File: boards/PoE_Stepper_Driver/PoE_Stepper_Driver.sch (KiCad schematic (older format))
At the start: 37 parts, among them J4 Programming, J5 48V In, J6 12V, 3V3 Out, J7 PHY Data, J8 SPI Data, SW3 SW_Push, U3 STM32F407VETx, U4 NCP1117, U5 E48SC12010, Y1 8MHz

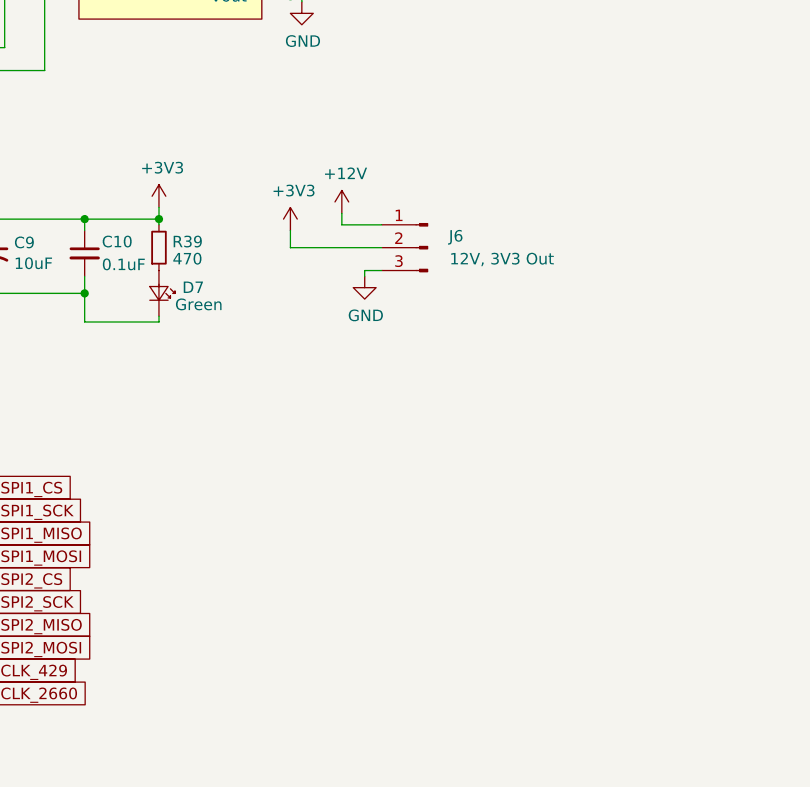
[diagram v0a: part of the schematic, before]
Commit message: finished 2660 planes
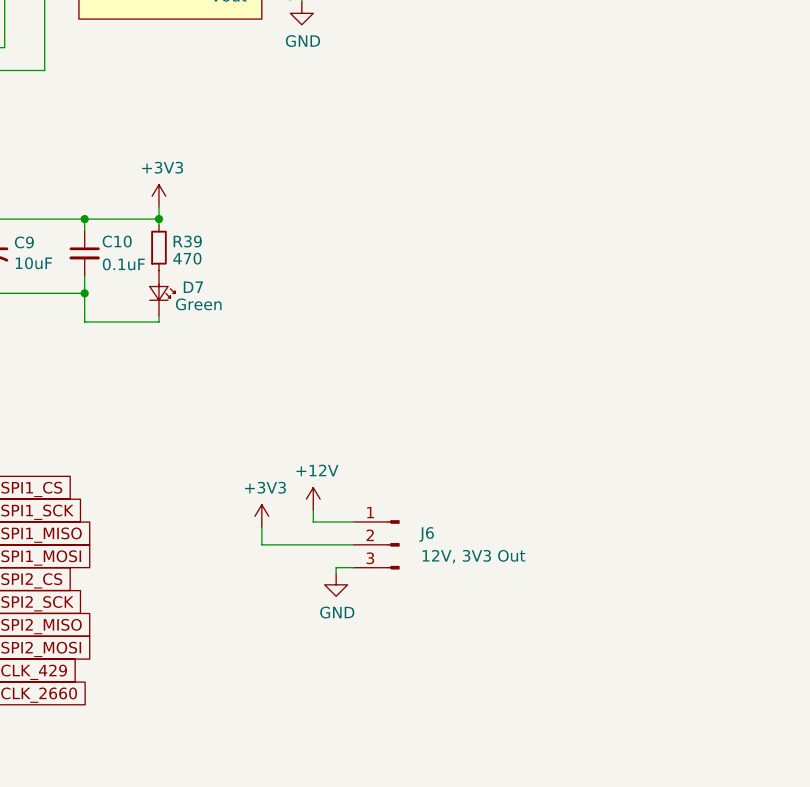
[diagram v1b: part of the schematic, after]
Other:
- moved on the sheet: J6
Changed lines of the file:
@@
 L Connector:Conn_01x03_Male J6
 U 1 1 6262632C
-P 10325 3475
+P 10200 4775
 AR Path="/6262632C" Ref="J6"  Part="1"
 AR Path="/620ECB3C/6262632C" Ref="J?"  Part="1"
-F 0 "J6" H 10200 3525 50  0000 C CNN
-F 1 "12V, 3V3 Out" H 10000 3425 50  0000 C CNN
-F 2 "Connector_PinHeader_2.54mm:PinHeader_1x03_P2.54mm_Vertical" H 10325 3475 50  0001 C CNN
-F 3 "~" H 10325 3475 50  0001 C CNN
-	1    10325 3475
+F 0 "J6" H 10075 4825 50  0000 C CNN
+F 1 "12V, 3V3 Out" H 9875 4725 50  0000 C CNN
+F 2 "Connector_PinHeader_2.54mm:PinHeader_1x03_P2.54mm_Vertical" H 10200 4775 50  0001 C CNN
+F 3 "~" H 10200 4775 50  0001 C CNN
+	1    10200 4775
 	-1   0    0    -1
 $EndComp
@@
 L power:GND #PWR058
 U 1 1 626508B2
-P 10050 3600
-F 0 "#PWR058" H 10050 3350 50  0001 C CNN
-F 1 "GND" H 10055 3427 50  0000 C CNN
-F 2 "" H 10050 3600 50  0001 C CNN
-F 3 "" H 10050 3600 50  0001 C CNN
-	1    10050 3600
+P 9925 4900
+F 0 "#PWR058" H 9925 4650 50  0001 C CNN
+F 1 "GND" H 9930 4727 50  0000 C CNN
+F 2 "" H 9925 4900 50  0001 C CNN
+F 3 "" H 9925 4900 50  0001 C CNN
+	1    9925 4900
 	1    0    0    -1
 $EndComp
 Wire Wire Line
-	10125 3575 10050 3575
+	10000 4875 9925 4875
 Wire Wire Line
-	10050 3575 10050 3600
+	9925 4875 9925 4900
 $Comp
 L power:+3V3 #PWR06
 U 1 1 6265E3AE
-P 9725 3400
-F 0 "#PWR06" H 9725 3250 50  0001 C CNN
-F 1 "+3V3" H 9740 3573 50  0000 C CNN
-F 2 "" H 9725 3400 50  0001 C CNN
-F 3 "" H 9725 3400 50  0001 C CNN
-	1    9725 3400
+P 9600 4700
+F 0 "#PWR06" H 9600 4550 50  0001 C CNN
+F 1 "+3V3" H 9615 4873 50  0000 C CNN
+F 2 "" H 9600 4700 50  0001 C CNN
+F 3 "" H 9600 4700 50  0001 C CNN
+	1    9600 4700
 	1    0    0    -1
 $EndComp
@@
 L power:+12V #PWR057
 U 1 1 626737A3
-P 9950 3325
-F 0 "#PWR057" H 9950 3175 50  0001 C CNN
-F 1 "+12V" H 9965 3498 50  0000 C CNN
-F 2 "" H 9950 3325 50  0001 C CNN
-F 3 "" H 9950 3325 50  0001 C CNN
-	1    9950 3325
+P 9825 4625
+F 0 "#PWR057" H 9825 4475 50  0001 C CNN
+F 1 "+12V" H 9840 4798 50  0000 C CNN
+F 2 "" H 9825 4625 50  0001 C CNN
+F 3 "" H 9825 4625 50  0001 C CNN
+	1    9825 4625
 	1    0    0    -1
 $EndComp
 Wire Wire Line
-	9950 3325 9950 3375
+	9825 4625 9825 4675
 Wire Wire Line
-	9950 3375 10125 3375
+	9825 4675 10000 4675
 Wire Wire Line
-	9725 3400 9725 3475
+	9600 4700 9600 4775
 Wire Wire Line
-	9725 3475 10125 3475
+	9600 4775 10000 4775
 Text GLabel 7450 5375 2    50   Input ~ 0
 CRS_DV
@@
 NoConn ~ 3225 6300
 $Comp
-L power:GND #PWR?
+L power:GND #PWR059
 U 1 1 628E2CDE
 P 2125 4050
-F 0 "#PWR?" H 2125 3800 50  0001 C CNN
+F 0 "#PWR059" H 2125 3800 50  0001 C CNN
 F 1 "GND" H 2130 3877 50  0000 C CNN
 F 2 "" H 2125 4050 50  0001 C CNN

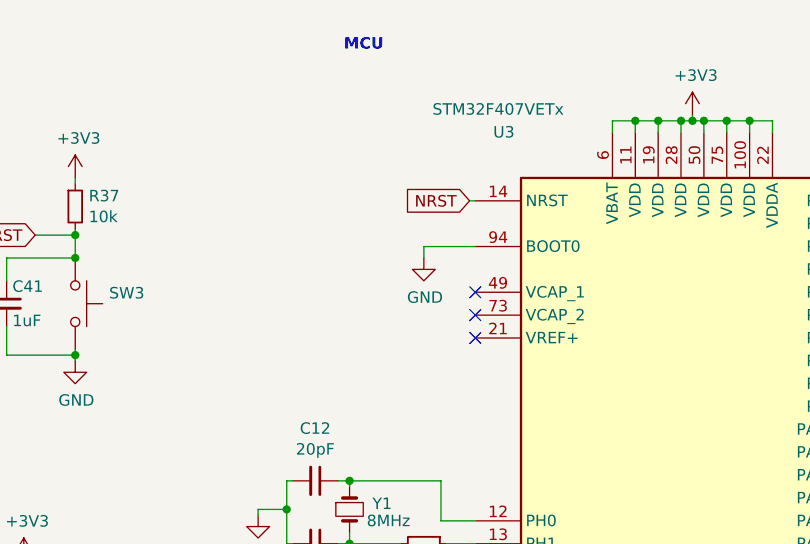
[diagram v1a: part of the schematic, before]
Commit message: added silkscreen info
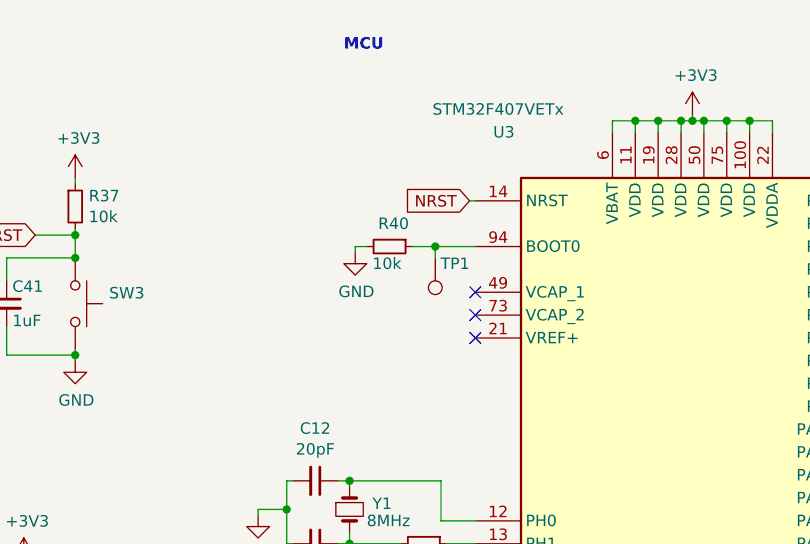
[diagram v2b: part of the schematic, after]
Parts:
- added R40: 10k, Resistor_SMD:R_0805_2012Metric_Pad1.15x1.40mm_HandSolder, symbol device:R_Small
- added TP1: BOOT0, TestPoint:TestPoint_Pad_1.0x1.0mm, symbol Connector:TestPoint
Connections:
- net GND: now also R40.2; no longer U3.94 (BOOT0)
- new net: R40.1, TP1.1, U3.94 (BOOT0)
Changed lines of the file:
@@
 L power:GND #PWR056
 U 1 1 625BB5F0
-P 3000 1750
-F 0 "#PWR056" H 3000 1500 50  0001 C CNN
-F 1 "GND" H 3005 1577 50  0000 C CNN
-F 2 "" H 3000 1750 50  0001 C CNN
-F 3 "" H 3000 1750 50  0001 C CNN
-	1    3000 1750
-	1    0    0    -1
-$EndComp
-Wire Wire Line
-	3225 1700 3000 1700
-Wire Wire Line
-	3000 1700 3000 1750
+P 2700 1725
+F 0 "#PWR056" H 2700 1475 50  0001 C CNN
+F 1 "GND" H 2705 1552 50  0000 C CNN
+F 2 "" H 2700 1725 50  0001 C CNN
+F 3 "" H 2700 1725 50  0001 C CNN
+	1    2700 1725
+	1    0    0    -1
+$EndComp
 $Comp
 L Connector:Conn_01x04_Male J4
@@
 	2125 3950 2125 4050
 Connection ~ 2125 3950
+$Comp
+L device:R_Small R40
+U 1 1 62AB9418
+P 2850 1700
+F 0 "R40" V 2750 1650 50  0000 L CNN
+F 1 "10k" V 2925 1625 50  0000 L CNN
+F 2 "Resistor_SMD:R_0805_2012Metric_Pad1.15x1.40mm_HandSolder" H 2850 1700 50  0001 C CNN
+F 3 "~" H 2850 1700 50  0001 C CNN
+	1    2850 1700
+	0    1    1    0
+$EndComp
+Wire Wire Line
+	2750 1700 2700 1700
+Wire Wire Line
+	2700 1700 2700 1725
+$Comp
+L Connector:TestPoint TP1
+U 1 1 62AE2994
+P 3050 1750
+F 0 "TP1" H 2900 1775 50  0000 L CNN
+F 1 "BOOT0" H 2775 1750 50  0001 L CNN
+F 2 "TestPoint:TestPoint_Pad_1.0x1.0mm" H 3250 1750 50  0001 C CNN
+F 3 "~" H 3250 1750 50  0001 C CNN
+	1    3050 1750
+	-1   0    0    1
+$EndComp
+Wire Wire Line
+	2950 1700 3050 1700
+Wire Wire Line
+	3050 1750 3050 1700
+Connection ~ 3050 1700
+Wire Wire Line
+	3050 1700 3225 1700
 $EndSCHEMATC

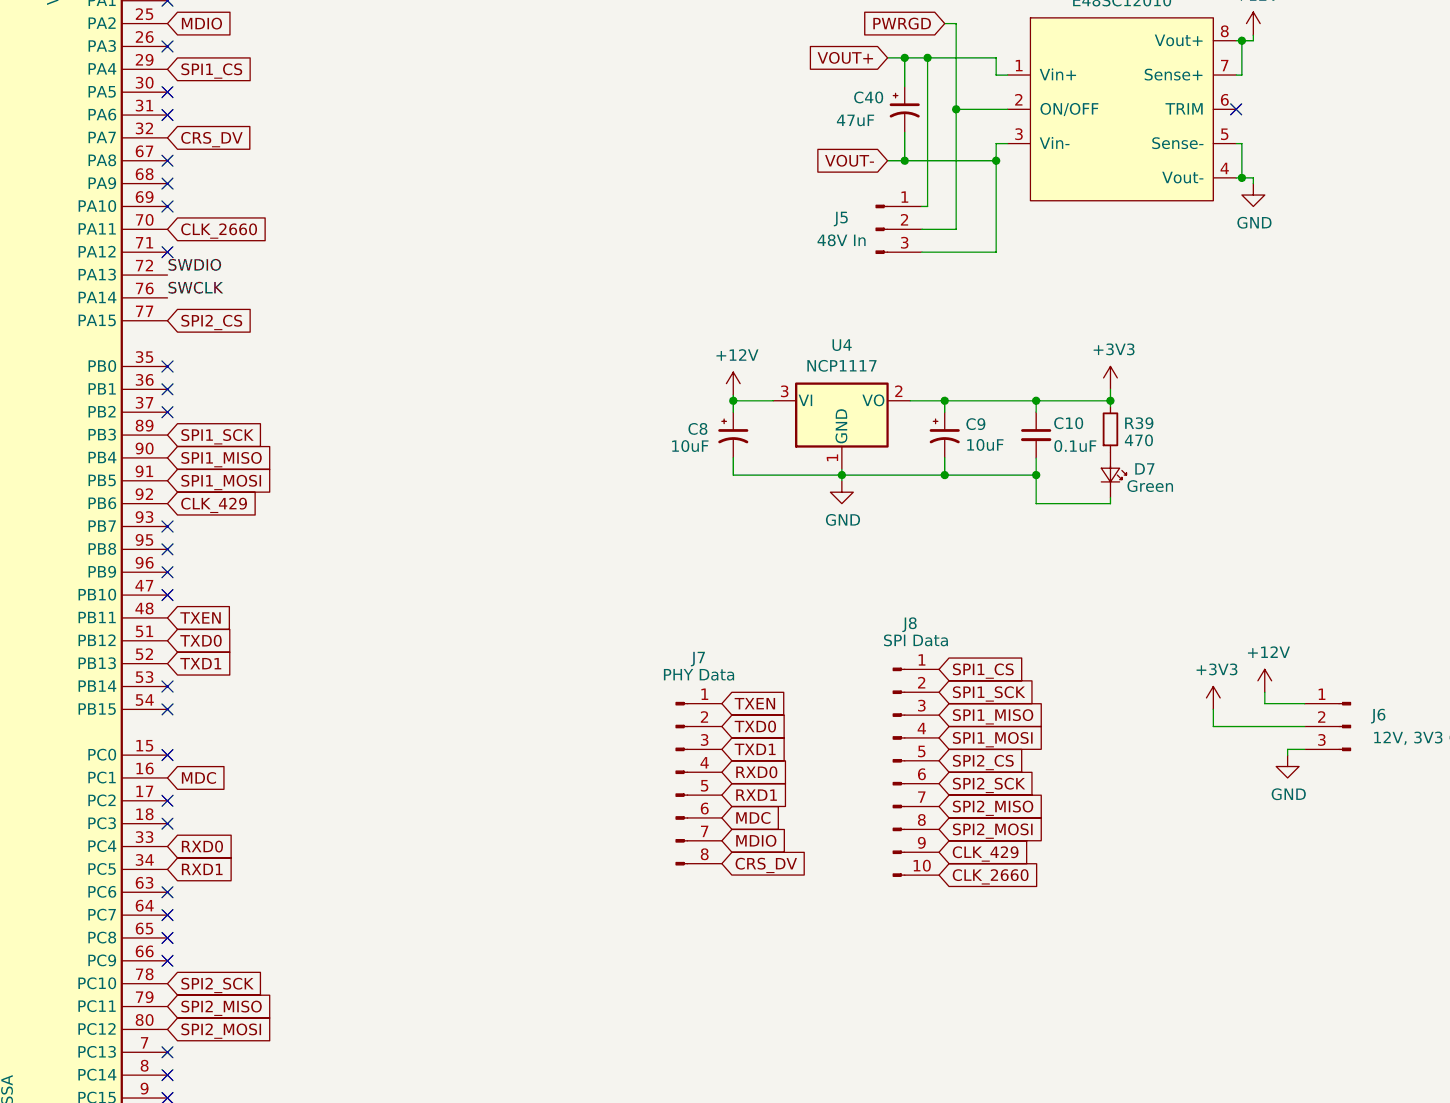
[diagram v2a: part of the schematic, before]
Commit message: added UART
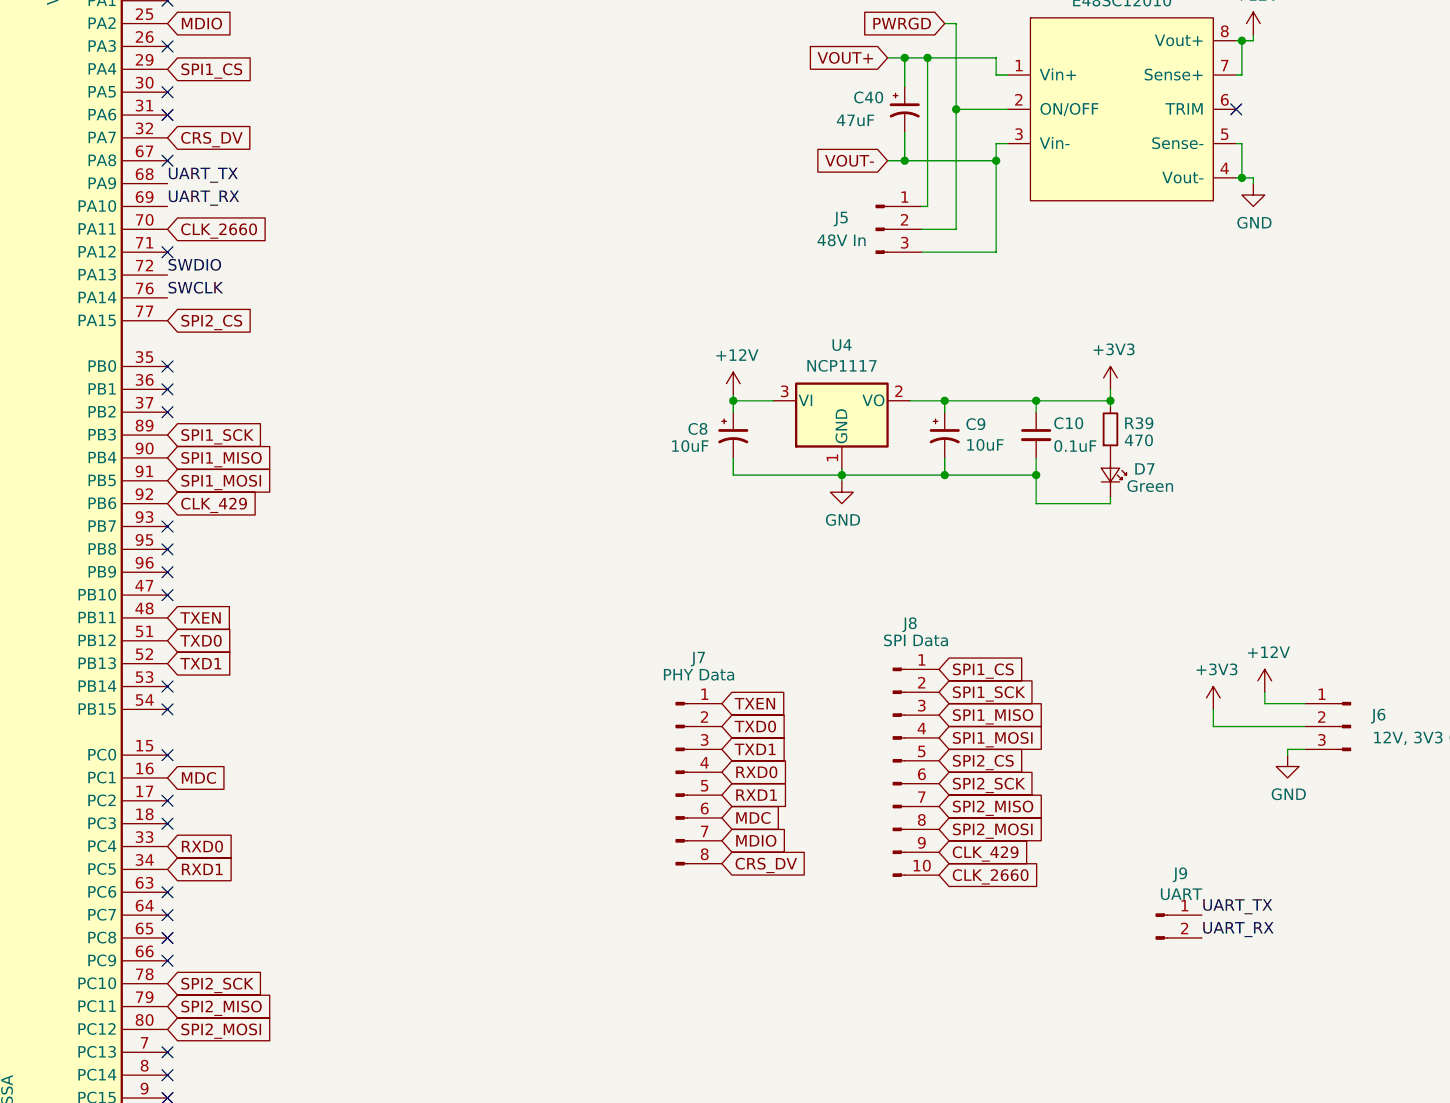
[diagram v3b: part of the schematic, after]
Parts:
- added J9: UART, Connector_PinHeader_2.54mm:PinHeader_1x02_P2.54mm_Vertical, symbol Connector:Conn_01x02_Male
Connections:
- net UART_TX: now reaches U3.68 (PA9)
- net UART_TX: now also J9.1 (Pin_1)
- net UART_RX: now reaches U3.69 (PA10)
- net UART_RX: now also J9.2 (Pin_2)
- no-connect marks 61 -> 59
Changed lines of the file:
@@
 NoConn ~ 5025 6300
 NoConn ~ 5025 2300
-NoConn ~ 5025 2400
-NoConn ~ 5025 2500
 NoConn ~ 5025 2700
 NoConn ~ 5025 3400
@@
 Wire Wire Line
 	3050 1700 3225 1700
+Text Label 5025 2400 0    50   ~ 0
+UART_TX
+Text Label 5025 2500 0    50   ~ 0
+UART_RX
+$Comp
+L Connector:Conn_01x02_Male J9
+U 1 1 62B51628
+P 9350 5600
+F 0 "J9" H 9458 5781 50  0000 C CNN
+F 1 "UART" H 9458 5690 50  0000 C CNN
+F 2 "Connector_PinHeader_2.54mm:PinHeader_1x02_P2.54mm_Vertical" H 9350 5600 50  0001 C CNN
+F 3 "~" H 9350 5600 50  0001 C CNN
+	1    9350 5600
+	1    0    0    -1
+$EndComp
+Text Label 9550 5600 0    50   ~ 0
+UART_TX
+Text Label 9550 5700 0    50   ~ 0
+UART_RX
 $EndSCHEMATC

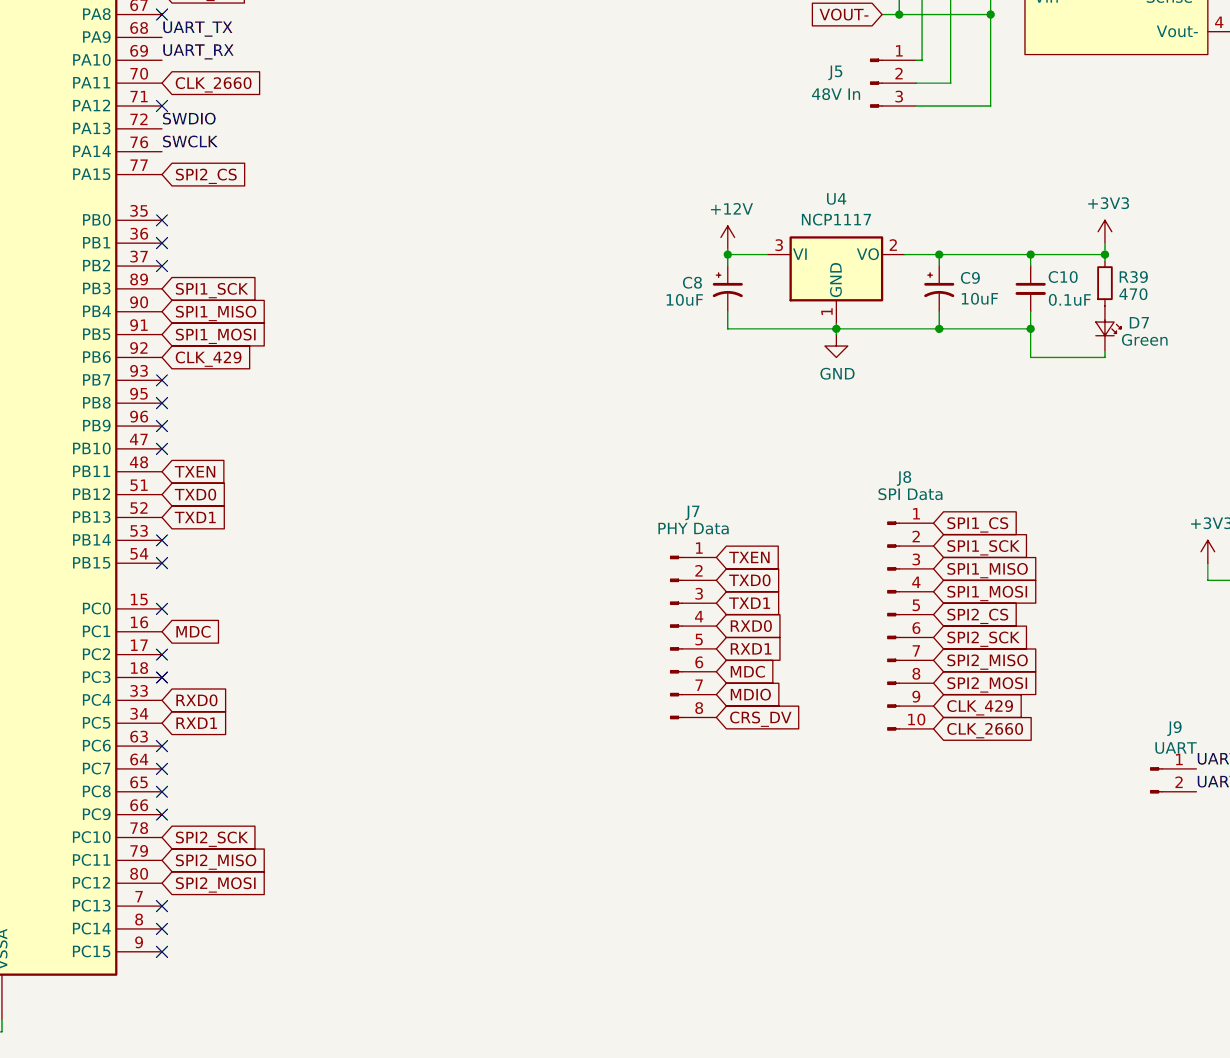
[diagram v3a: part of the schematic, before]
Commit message: added timers for trinamic clks
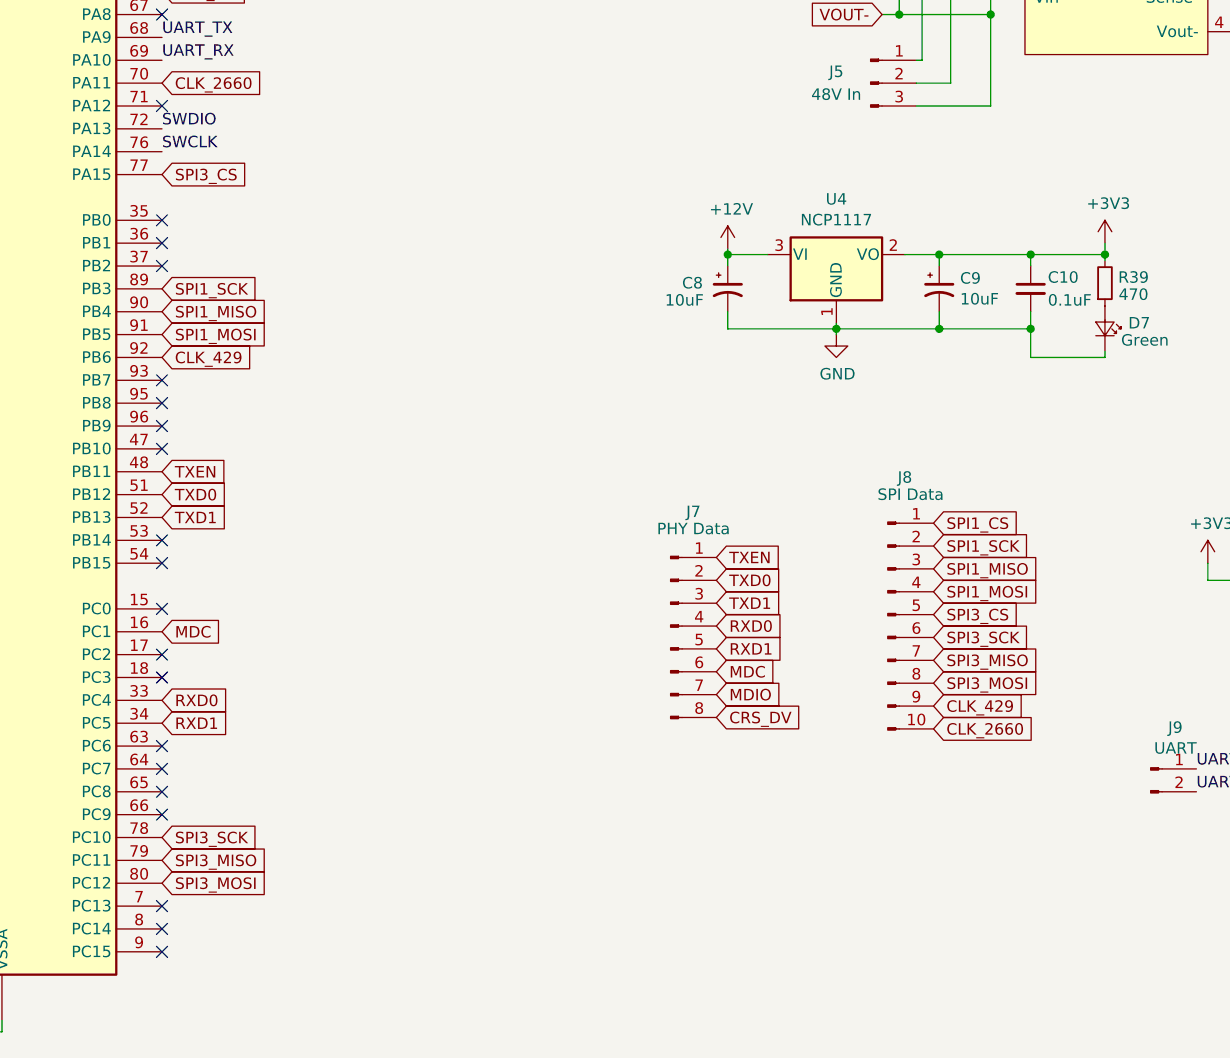
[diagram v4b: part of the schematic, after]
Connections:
- net SPI2_CS renamed SPI3_CS
- net SPI2_MISO renamed SPI3_MISO
- net SPI2_MOSI renamed SPI3_MOSI
- net SPI2_SCK renamed SPI3_SCK
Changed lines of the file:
@@
 CLK_2660
 Text GLabel 5025 5900 2    50   Input ~ 0
-SPI2_SCK
+SPI3_SCK
 Text GLabel 5025 6100 2    50   Input ~ 0
-SPI2_MOSI
+SPI3_MOSI
 Text GLabel 5025 3000 2    50   Input ~ 0
-SPI2_CS
+SPI3_CS
 $Comp
 L device:R_Small R1
@@
 MDC
 Text GLabel 5025 6000 2    50   Input ~ 0
-SPI2_MISO
+SPI3_MISO
 Text Notes 2650 850  0    50   ~ 10
 MCU
@@
 SPI1_CS
 Text GLabel 8400 5025 2    50   Input ~ 0
-SPI2_SCK
+SPI3_SCK
 Text GLabel 8400 5225 2    50   Input ~ 0
-SPI2_MOSI
+SPI3_MOSI
 Text GLabel 8400 5125 2    50   Input ~ 0
-SPI2_MISO
+SPI3_MISO
 Text GLabel 8400 4925 2    50   Input ~ 0
-SPI2_CS
+SPI3_CS
 Text GLabel 8400 5325 2    50   Input ~ 0
 CLK_429
